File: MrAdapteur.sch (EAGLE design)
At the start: 19 parts, among them X1 1751248

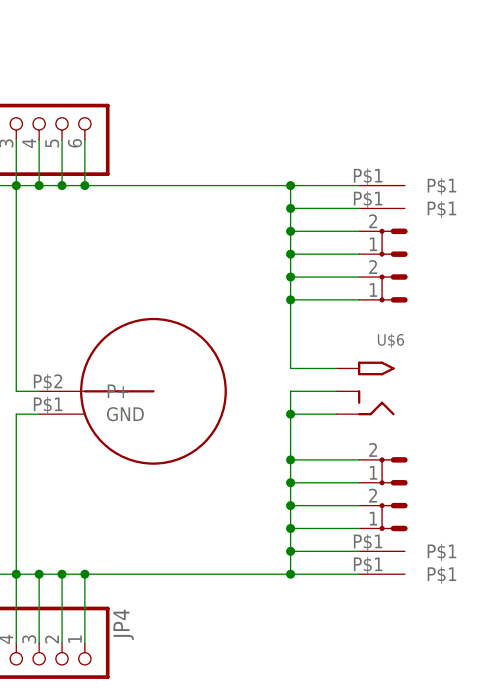
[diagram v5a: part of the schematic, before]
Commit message: Fixed hole size for wire clips, added stop mask for the UL/Manufacturing marks
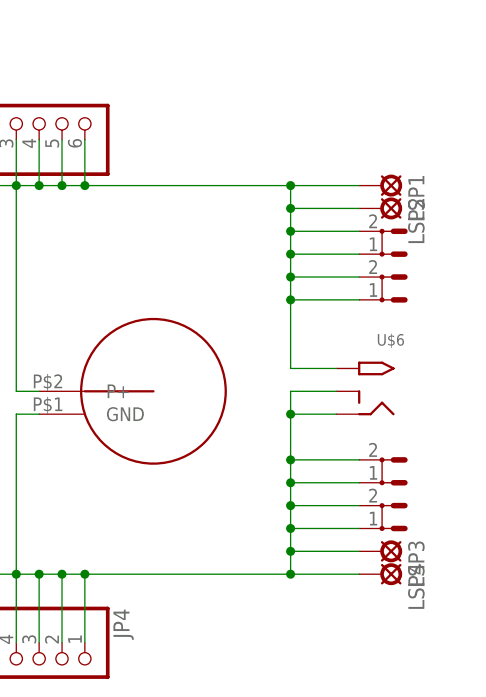
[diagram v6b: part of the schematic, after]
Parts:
- removed U$10, U$11, U$8, U$9: SOLPAD07, 4mm:SOLPAD07
- added LSP1, LSP2, LSP3, LSP4: LSP11, solpad:LSP11
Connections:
- net N$1: now also LSP1.MP, LSP2.MP; no longer U$10.P$1, U$8.P$1
- net N$3: now also LSP3.MP, LSP4.MP; no longer U$11.P$1, U$9.P$1
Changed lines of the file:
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@@
 <part name="WASHERSM6" library="dummy" deviceset="DUMMY" device=""/>
 <part name="SCREWSM3" library="dummy" deviceset="DUMMY" device=""/>
-<part name="U$8" library="4mm" deviceset="SOLPAD07" device=""/>
-<part name="U$9" library="4mm" deviceset="SOLPAD07" device=""/>
-<part name="U$10" library="4mm" deviceset="SOLPAD07" device=""/>
-<part name="U$11" library="4mm" deviceset="SOLPAD07" device=""/>
+<part name="LSP1" library="solpad" deviceset="LSP11" device=""/>
+<part name="LSP2" library="solpad" deviceset="LSP11" device=""/>
+<part name="LSP3" library="solpad" deviceset="LSP11" device=""/>
+<part name="LSP4" library="solpad" deviceset="LSP11" device=""/>
 </parts>
 <sheets>
@@
 <instance part="WASHERSM6" gate="G$1" x="15.24" y="96.52"/>
 <instance part="SCREWSM3" gate="G$1" x="15.24" y="88.9"/>
-<instance part="U$8" gate="G$1" x="157.48" y="83.82"/>
-<instance part="U$9" gate="G$1" x="157.48" y="40.64"/>
-<instance part="U$10" gate="G$1" x="157.48" y="81.28"/>
-<instance part="U$11" gate="G$1" x="157.48" y="43.18"/>
+<instance part="LSP1" gate="1" x="157.48" y="83.82" rot="R270"/>
+<instance part="LSP2" gate="1" x="157.48" y="81.28" rot="R270"/>
+<instance part="LSP3" gate="1" x="157.48" y="43.18" rot="R270"/>
+<instance part="LSP4" gate="1" x="157.48" y="40.64" rot="R270"/>
 </instances>
 <busses>
@@
 <wire x1="147.32" y1="83.82" x2="154.94" y2="83.82" width="0.1524" layer="91"/>
 <junction x="147.32" y="83.82"/>
-<pinref part="U$8" gate="G$1" pin="P$1"/>
-<pinref part="U$10" gate="G$1" pin="P$1"/>
 <wire x1="154.94" y1="81.28" x2="147.32" y2="81.28" width="0.1524" layer="91"/>
 <junction x="147.32" y="81.28"/>
+<pinref part="LSP2" gate="1" pin="MP"/>
+<pinref part="LSP1" gate="1" pin="MP"/>
 </segment>
 </net>
@@
 <pinref part="U$6" gate="G$1" pin="RING"/>
 <pinref part="U$6" gate="G$1" pin="RING_SW"/>
-<pinref part="U$9" gate="G$1" pin="P$1"/>
 <wire x1="147.32" y1="40.64" x2="154.94" y2="40.64" width="0.1524" layer="91"/>
 <junction x="147.32" y="40.64"/>
-<pinref part="U$11" gate="G$1" pin="P$1"/>
 <wire x1="154.94" y1="43.18" x2="147.32" y2="43.18" width="0.1524" layer="91"/>
 <junction x="147.32" y="43.18"/>
+<pinref part="LSP3" gate="1" pin="MP"/>
+<pinref part="LSP4" gate="1" pin="MP"/>
 </segment>
 </net>
